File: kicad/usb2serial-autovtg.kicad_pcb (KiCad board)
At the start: 2 copper layers, 24 x 18 mm, 38 parts, among them J2 Conn_01x04, J3 USB_C_Receptacle_USB2.0, U1 FT234XD, U3 74LVC1G17GW, U5 LMV358AIDGKR, U6 74LVC1G17GW

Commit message: 1.2V: wip
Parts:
- removed D4: BZX84C2V4LT1, Package_TO_SOT_SMD:SOT-23
- removed R15: 120, Resistor_SMD:R_0402_1005Metric
- removed U3, U6: 74LVC1G17GW, Package_SO:TSOP-5_1.65x3.05mm_P0.95mm
- added U2: 74LVC1T45GW, Package_TO_SOT_SMD:SOT-363_SC-70-6, F.Cu at (152.6, 76.8)
- added U4: 74LVC1T45GW, Package_TO_SOT_SMD:SOT-363_SC-70-6, F.Cu at (152.8, 65.5)
- added U7: TLV74112PDBVR, Package_TO_SOT_SMD:SOT-23-5, F.Cu at (144.7, 71.4)
- C5: value 0.1u -> 1u
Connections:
- C5 pad 1: +2V5 -> +1V2
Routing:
- net +2V5: track 7.19 -> 0.00 mm
- net +1V2: track 0.00 -> 6.37 mm
- net Net-(U1-TXD): track 7.78 -> 3.39 mm
- net Net-(U2-B): track 2.25 -> 0.00 mm
- net GND: track 31.6 -> 29.6 mm, vias 18 -> 16
- net +3V3: track 19.8 -> 21.3 mm
- net Net-(U1-RXD): track 5.61 -> 4.83 mm, vias 2 -> 1

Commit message: wip
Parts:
- added C7: 0.1u/10V, Capacitor_SMD:C_0402_1005Metric, F.Cu at (151.3, 74.5)
- moved U4 6.86 mm to (152.3, 72.4)
- moved U2 0.76 mm to (152.4, 77.6)
- moved R4 0.70 mm to (151.3, 75.6)
- moved R5 0.70 mm to (153.3, 74.5)
- moved R11 0.70 mm to (153.3, 75.6)
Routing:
- net Net-(D1-K): track 17.4 -> 11.9 mm
- net +3V3: track 21.3 -> 26.6 mm
- net Net-(U4-B): track 10.9 -> 6.92 mm
- net Net-(U1-TXD): track 3.39 -> 6.22 mm, vias 0 -> 2
- net /TXOUT: track 2.75 -> 0.00 mm
- net /RXIN: track 2.67 -> 0.00 mm
- net Net-(U2-B): track 0.00 -> 2.11 mm
- net Net-(U1-RXD): track 4.83 -> 3.03 mm
- net +1V2: track 6.37 -> 5.04 mm
- net GND: track 29.6 -> 30.4 mm, vias 16 -> 17
- net Net-(U2-VCCB): track 2.80 -> 3.41 mm

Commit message: finalize rev3
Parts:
- C5: value 1u -> 4.7u/10V
- moved C5 0.48 mm to (150.2, 71.1), turned to -90 degrees
- moved U4 0.29 mm to (152.2, 72.2)
- moved C7 0.15 mm to (151.2, 74.5)
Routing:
- net Net-(D1-K): track 11.9 -> 19.9 mm, vias 0 -> 2
- net +3V3: track 26.6 -> 31.1 mm
- net Net-(U4-B): track 6.92 -> 11.3 mm
- net Net-(U1-RXD): track 3.03 -> 7.00 mm, vias 1 -> 2
- net /RXIN: track 0.00 -> 2.96 mm
- net /TXOUT: track 0.00 -> 2.46 mm
- net GND: track 30.4 -> 32.7 mm, vias 17 -> 19
- net +1V2: track 5.04 -> 5.97 mm
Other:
- board text added: "FT234 autoVtg v3 znu 2024"
- board text added: "IO Voltage: 1.2V to 5V"
- board text removed: "FT234 autoVtg v2 znu 2023"

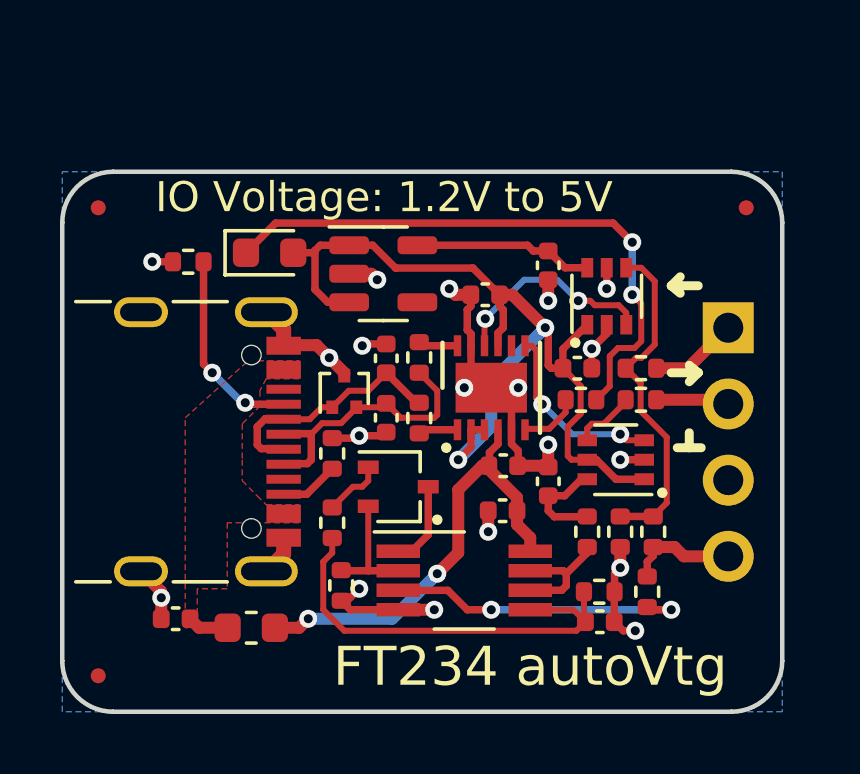
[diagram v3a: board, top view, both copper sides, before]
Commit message: modify Vtg silkscreen text
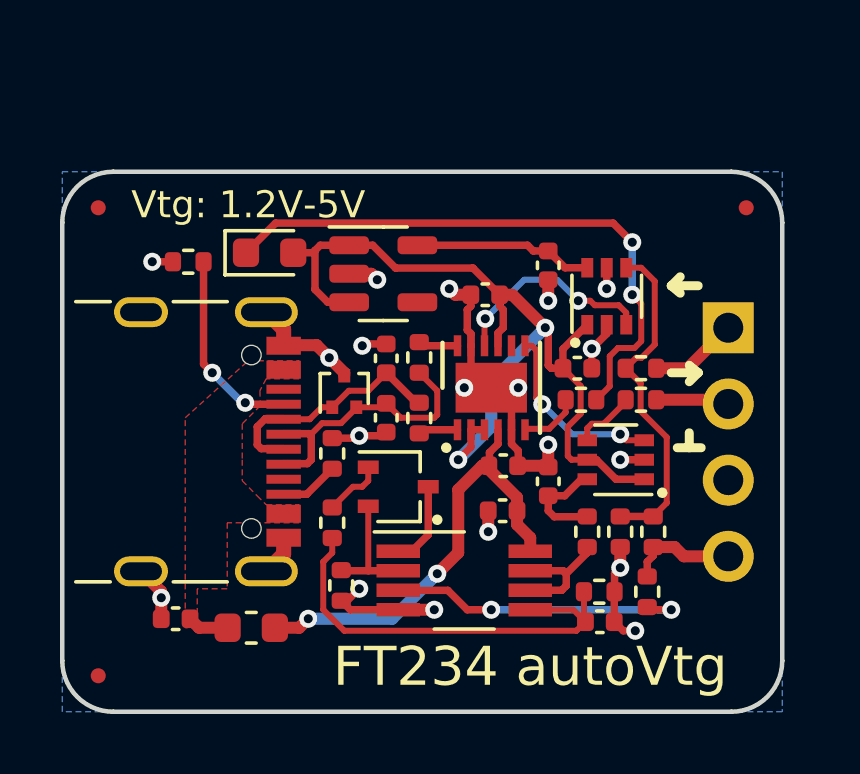
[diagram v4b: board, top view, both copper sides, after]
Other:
- board text added: "Vtg: 1.2V-5V"
- board text removed: "IO Voltage: 1.2V to 5V"
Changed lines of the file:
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@@
     (effects (font (size 1.3 1.3) (thickness 0.25)))
   )
-  (gr_text "IO Voltage: 1.2V to 5V" (at 137.1 68.85) (layer "F.SilkS")
-    (effects (font (size 1 1) (thickness 0.2)) (justify left))
+  (gr_text "Vtg: 1.2V-5V" (at 136.3 69.1) (layer "F.SilkS")
+    (effects (font (size 0.9 0.9) (thickness 0.2)) (justify left))
   )
   (segment (start 143.9 76.8) (end 144.68 76.8) (width 0.25) (layer "F.Cu") (net 1))
